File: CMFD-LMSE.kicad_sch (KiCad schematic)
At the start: 52 parts

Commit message: 回路図（ひとまず完成）
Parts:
- added J1, J10, J11, J12, J7, J8, J9: Conn_01x02, DF1B-2P-2.5DSA:CON2_1X2_U_DF1BZ_HIR, symbol Connector_Generic:Conn_01x02
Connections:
- net GND: now also J1.2 (Pin_2), J10.2 (Pin_2), J11.2 (Pin_2), J12.2 (Pin_2), J7.2 (Pin_2), J8.2 (Pin_2), J9.2 (Pin_2)
- net MCU/GPIO_4: now reaches R8.1
- net MCU/GPIO_9: now reaches R13.1
- net MCU/GPIO_2: now reaches R6.1
- net MCU/GPIO_3: now reaches R7.1
- net MCU/GPIO_6: now reaches R10.1
- net MCU/GPIO_7: now reaches R11.1
- net MCU/GPIO_5: now reaches R9.1
- net MCU/GPIO_8: now reaches R12.1
- net MCU/GPIO_1: now reaches R5.1
- new net MCU/GPIO_LM_1: J1.1 (Pin_1)
- new net MCU/GPIO_LM_2: J7.1 (Pin_1)
- new net MCU/GPIO_LM_3: J8.1 (Pin_1)
- new net MCU/GPIO_LM_4: J9.1 (Pin_1)
- new net MCU/GPIO_LM_5: J10.1 (Pin_1)
- new net MCU/GPIO_LM_6: J11.1 (Pin_1)
- new net MCU/GPIO_LM_7: J12.1 (Pin_1)
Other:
- sheet MCU ports: added GPIO_1, GPIO_2, GPIO_3, GPIO_4, GPIO_5, GPIO_6, GPIO_7, GPIO_8, GPIO_9, GPIO_LM_1, GPIO_LM_2, GPIO_LM_3, GPIO_LM_4, GPIO_LM_5, GPIO_LM_6, GPIO_LM_7; removed none

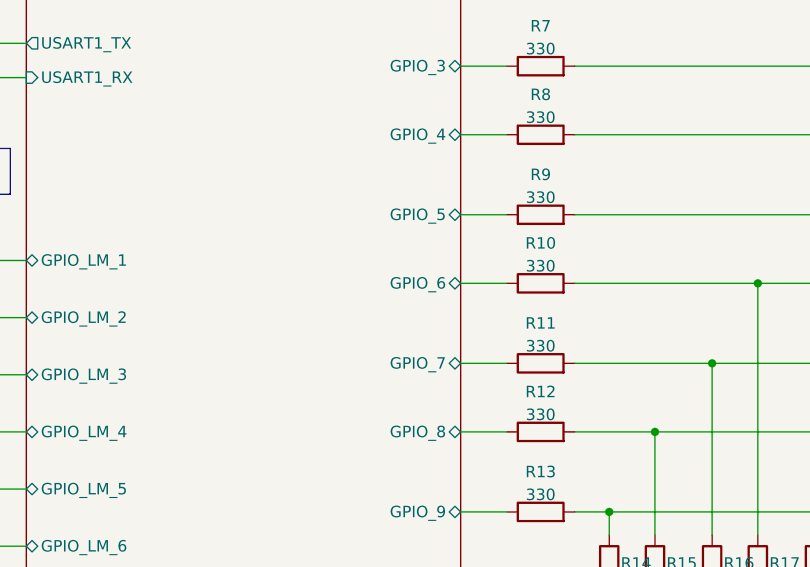
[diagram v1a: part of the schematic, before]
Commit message: 抵抗器のフットプリントを策定
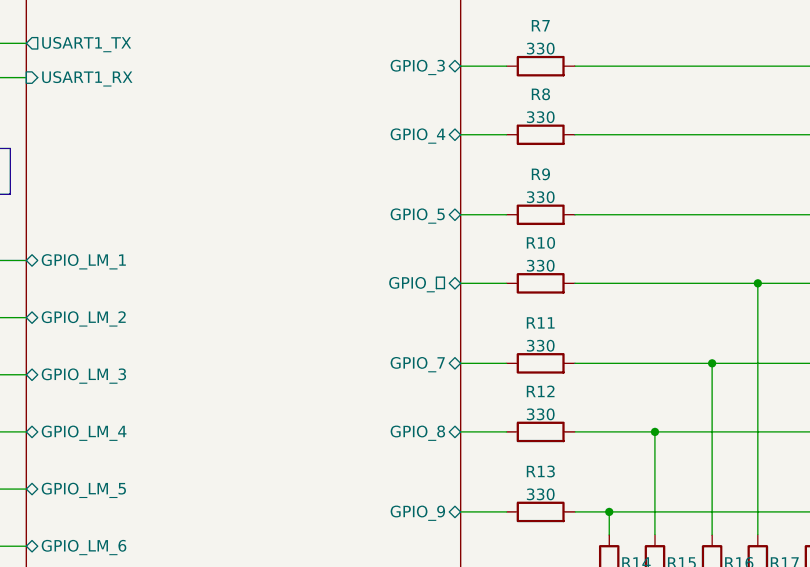
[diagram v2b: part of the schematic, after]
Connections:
- net MCU/GPIO_6 renamed MCU/GPIO_６
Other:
- sheet MCU ports: added GPIO_６; removed GPIO_6
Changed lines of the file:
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@@
-			)
-		)
-		(pin "GPIO_6" bidirectional
-			(at 139.7 92.71 0)
-			(effects
-				(font
-					(size 1.27 1.27)
-				)
-				(justify right)
 			)
 		)
@@
 			)
 		)
+		(pin "GPIO_６" bidirectional
+			(at 139.7 92.71 0)
+			(effects
+				(font
+					(size 1.27 1.27)
+				)
+				(justify right)
+			)
+		)
